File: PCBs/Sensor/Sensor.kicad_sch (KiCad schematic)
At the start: 7 parts, among them J1 RJ45, J2 RJ45, U1 ATtiny85-20P

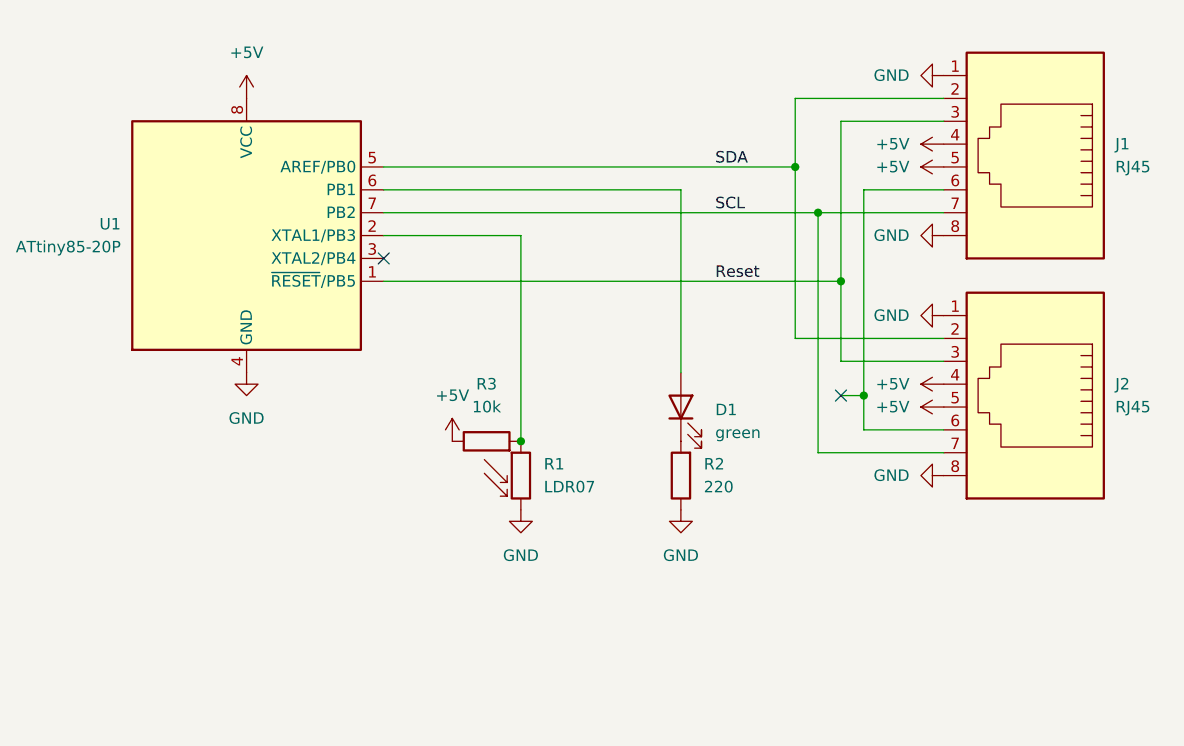
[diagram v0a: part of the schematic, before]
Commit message: update RJ45 pins and pwr_flag
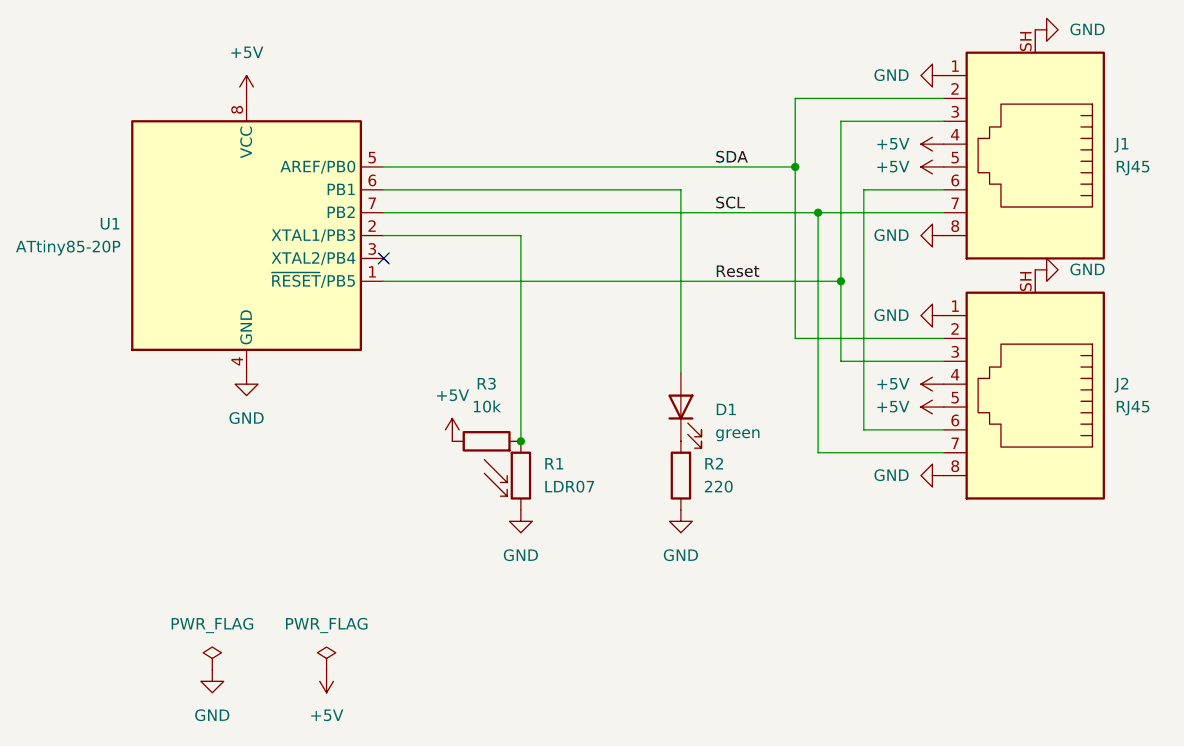
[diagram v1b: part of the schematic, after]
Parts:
- J1, J2: symbol Connector:RJ45 -> Connector:RJ45_Shielded
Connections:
- net GND: now also J1.SH, J2.SH
- no-connect marks 2 -> 1

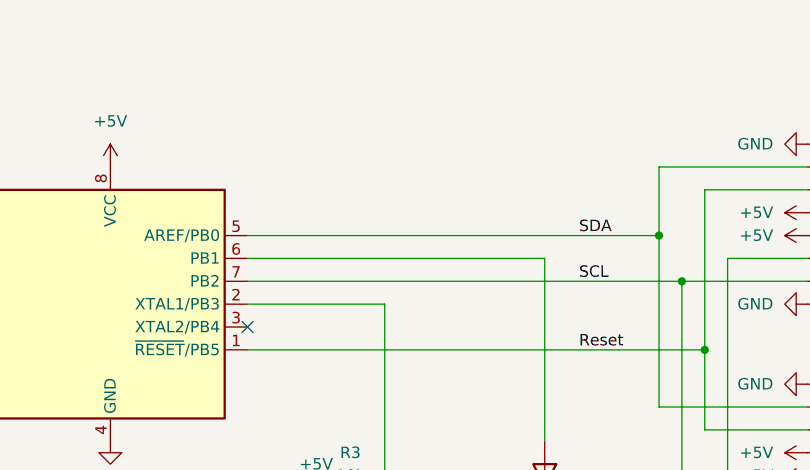
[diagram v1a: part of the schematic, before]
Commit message: integrate buzzer PCB into Sensor
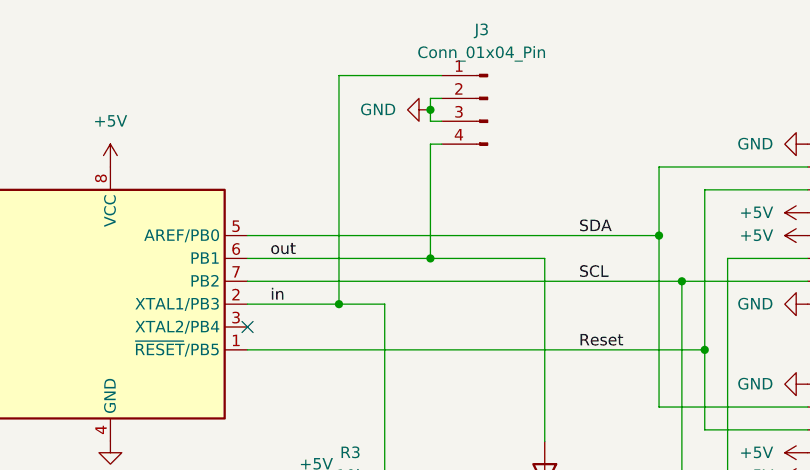
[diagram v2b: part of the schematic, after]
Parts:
- added J3: Conn_01x04_Pin, Connector_PinHeader_2.54mm:PinHeader_1x04_P2.54mm_Vertical, symbol Connector:Conn_01x04_Pin
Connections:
- net GND: now also J3.2 (Pin_2), J3.3 (Pin_3)
- net in: now reaches R1.1, R3.2, U1.2 (XTAL1/PB3)
- net in: now also J3.1 (Pin_1)
- net out: now reaches D1.2 (A), U1.6 (PB1)
- net out: now also J3.4 (Pin_4)

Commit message: Update README
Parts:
- D1: value green -> LED
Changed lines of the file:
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@@
 			)
 		)
-		(property "Value" "green"
+		(property "Value" "LED"
 			(at 106.68 87.9474 90)
 			(effects

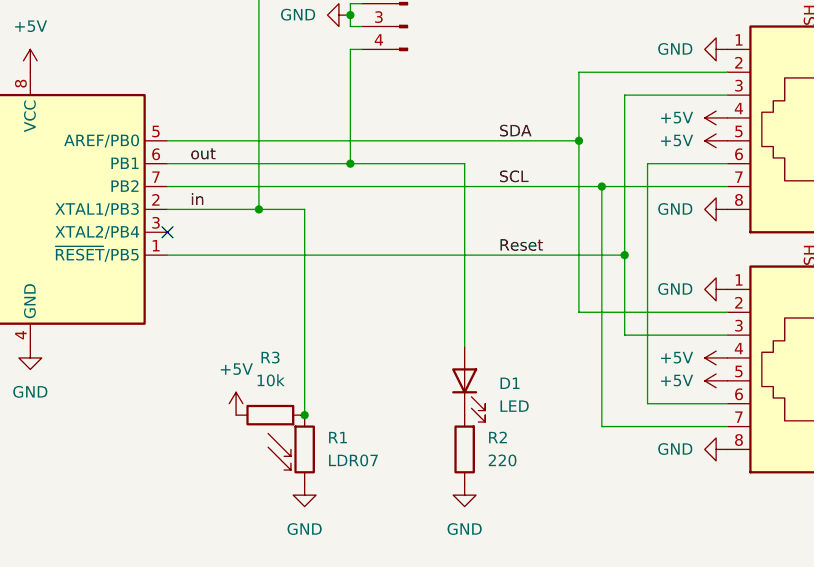
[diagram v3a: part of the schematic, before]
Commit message: added jumper pad
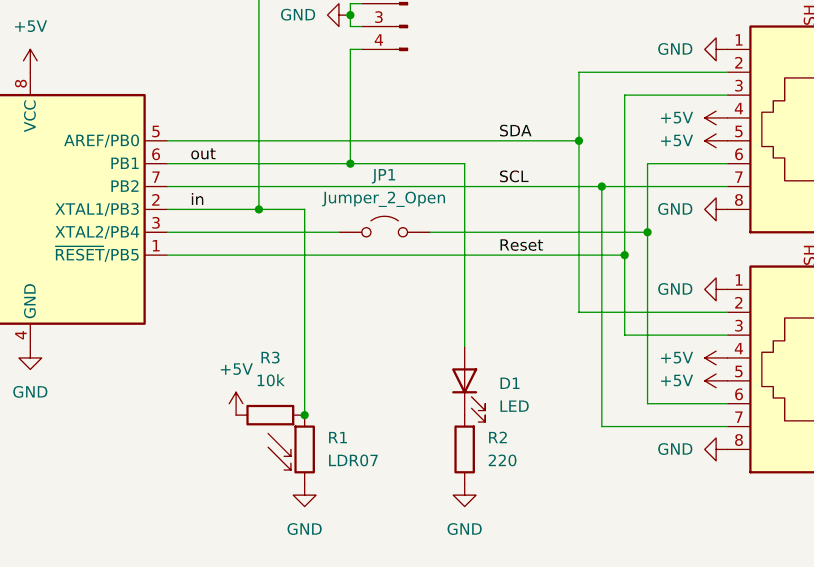
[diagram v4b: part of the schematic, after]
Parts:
- added JP1: Jumper_2_Open, Jumper:SolderJumper-2_P1.3mm_Open_TrianglePad1.0x1.5mm, symbol Jumper:Jumper_2_Open
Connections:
- net at J1.6, J2.6: now also JP1.2 (B)
- net at U1.3 (XTAL2/PB4): now also JP1.1 (A)
- no-connect marks 1 -> 0
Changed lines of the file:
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@@
+	)
+	(junction
+		(at 123.19 68.58)
+		(diameter 0)
+		(color 0 0 0 0)
 	)
 	(junction
@@
 		(color 0 0 0 0)
 	)
-	(no_connect
-		(at 69.85 68.58)
+	(wire
+		(pts
+			(xy 99.06 68.58) (xy 123.19 68.58)
+		)
+		(stroke
+			(width 0)
+			(type default)
+		)
 	)
 	(wire
@@
 	(wire
 		(pts
+			(xy 69.85 68.58) (xy 88.9 68.58)
+		)
+		(stroke
+			(width 0)
+			(type default)
+		)
+	)
+	(wire
+		(pts
 			(xy 118.11 63.5) (xy 132.08 63.5)
 		)
@@
 	(wire
 		(pts
-			(xy 123.19 60.96) (xy 123.19 87.63)
+			(xy 123.19 60.96) (xy 123.19 68.58)
 		)
 		(stroke
@@
 		(pts
 			(xy 90.17 48.26) (xy 90.17 60.96)
+		)
+		(stroke
+			(width 0)
+			(type default)
+		)
+	)
+	(wire
+		(pts
+			(xy 123.19 68.58) (xy 123.19 87.63)
 		)
 		(stroke
@@
 					(unit 1)
 				)
+			)
+		)
+	)
+	(symbol
+		(lib_id "Jumper:Jumper_2_Open")
+		(at 93.98 68.58 0)
+		(unit 1)
+		(exclude_from_sim yes)
+		(in_bom yes)
+		(on_board yes)
+		(dnp no)
+		(fields_autoplaced yes)
+		(property "Reference" "JP1"
+			(at 93.98 62.23 0)
+			(effects
+				(font
+					(size 1.27 1.27)
+				)
+			)
+		)
+		(property "Value" "Jumper_2_Open"
+			(at 93.98 64.77 0)
+			(effects
+				(font
+					(size 1.27 1.27)
+				)
+			)
+		)
+		(property "Footprint" "Jumper:SolderJumper-2_P1.3mm_Open_TrianglePad1.0x1.5mm"
+			(at 93.98 68.58 0)
+			(effects
+				(font
+					(size 1.27 1.27)
+				)
+				(hide yes)
+			)
+		)
+		(property "Datasheet" "~"
+			(at 93.98 68.58 0)
+			(effects
+				(font
+					(size 1.27 1.27)
+				)
+				(hide yes)
+			)
+		)
+		(property "Description" "Jumper, 2-pole, open"
+			(at 93.98 68.58 0)
+			(effects
+				(font
+					(size 1.27 1.27)
+				)
+				(hide yes)
+			)
+		)
+		(pin "1"
+		)
+		(pin "2"
+		)
+		(instances
+			(project ""
+				(path "/799e09d1-2985-4565-afc4-1243d8c883bb"
+					(reference "JP1")
+					(unit 1)
+				)

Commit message: update sensor
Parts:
- removed J1: RJ45, Library:WR-MJ Modular Jack Horizontal Shielded w. EMI Panel Finger 8P8C Tab Up, symbol Connector:RJ45_Shielded
- removed JP1: Jumper_2_Open, Jumper:SolderJumper-2_P1.3mm_Open_TrianglePad1.0x1.5mm, symbol Jumper:Jumper_2_Open
- added C1: 0.1μ, Capacitor_THT:C_Disc_D3.0mm_W1.6mm_P2.50mm, symbol Device:C
- added J3, J4: RJ45, Library:WR-MJ Modular Jack Horizontal Shielded w. EMI Panel Finger 8P8C Tab Up, symbol Connector:RJ45_Shielded
- added JP1: Jumper_2_Bridged, Jumper:SolderJumper-2_P1.3mm_Bridged_RoundedPad1.0x1.5mm, symbol Jumper:Jumper_2_Bridged
- added JP2: Jumper_2_Open, Jumper:SolderJumper-2_P1.3mm_Open_RoundedPad1.0x1.5mm, symbol Jumper:Jumper_2_Open
- renumbered J3 to J1, R3 to R1, R1 to R2, R2 to R3
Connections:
- net GND: now also J1.1 (Pin_1), R3.2, C1.2, J3.1, J3.8, J3.SH, J4.1, J4.8, J4.SH; no longer J1.3 (Pin_3), R3.1
- net in: now also J1.3 (Pin_3), R1.1; no longer J1.1 (Pin_1), R1.2
- net at J2.6: now also J3.6, J4.6, JP2.2 (B)
- net FU: now reaches U1.3 (XTAL2/PB4)
- net FU: now also JP2.1 (A)
- net at D1.1 (K): now also R3.1; no longer R3.2
- net +5V renamed +3.3V
- net +3.3V: now also R1.2, C1.1, J3.4, J3.5, J4.4, J4.5; no longer R1.1
- net Reset: no longer names the net of J2.3
- net Reset: now also J3.3, J4.3, JP1.2 (B); no longer U1.1 (~{RESET}/PB5)
- net SCL renamed SCL0
- net SCL0: now also J3.7, J4.7
- net SDA renamed SDA0
- net SDA0: now also J3.2, J4.2
- new net AT_RS: JP1.1 (A), U1.1 (~{RESET}/PB5)
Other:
- moved on the sheet: D1, J1, R1, R2, R3

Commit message: Update Sensor.kicad_sch
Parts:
- JP1: value Jumper_2_Bridged -> Jumper_2_Open; footprint Jumper:SolderJumper-2_P1.3mm_Bridged_RoundedPad1.0x1.5mm -> Jumper:SolderJumper-2_P1.3mm_Open_RoundedPad1.0x1.5mm; symbol Jumper:Jumper_2_Bridged -> Jumper:Jumper_2_Open
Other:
- moved on the sheet: JP1
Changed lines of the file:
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@@
 	)
 	(symbol
-		(lib_id "Jumper:Jumper_2_Bridged")
+		(lib_id "Jumper:Jumper_2_Open")
 		(at 207.01 83.82 0)
 		(unit 1)
@@
 		(fields_autoplaced yes)
 		(property "Reference" "JP1"
-			(at 207.01 78.74 0)
+			(at 207.01 77.47 0)
 			(effects
 				(font
@@
 			)
 		)
-		(property "Value" "Jumper_2_Bridged"
-			(at 207.01 81.28 0)
+		(property "Value" "Jumper_2_Open"
+			(at 207.01 80.01 0)
 			(effects
 				(font
@@
 			)
 		)
-		(property "Footprint" "Jumper:SolderJumper-2_P1.3mm_Bridged_RoundedPad1.0x1.5mm"
+		(property "Footprint" "Jumper:SolderJumper-2_P1.3mm_Open_RoundedPad1.0x1.5mm"
 			(at 207.01 83.82 0)
 			(effects
@@
 			)
 		)
-		(property "Description" "Jumper, 2-pole, closed/bridged"
+		(property "Description" "Jumper, 2-pole, open"
 			(at 207.01 83.82 0)
 			(effects
